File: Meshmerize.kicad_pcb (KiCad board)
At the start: 2 copper layers, 113.9 x 108.8 mm, 54 parts, among them J1 Conn_01x19_Male, J2 Conn_01x19_Male, J3 Conn_01x04_Female, M1 Motor_DC, M2 Motor_DC, U1 LM324, U2 ESP32-DEVKITC-32D, U3 TCRT5000, U4 TCRT5000, U5 MT3608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

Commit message: Added Logos
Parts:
- added G***: LOGO, logos:PCB_Power_Small, F.Cu at (183.6, 54.5)
- added G***: LOGO, logos:PCB-Power, B.Cu at (182.2, 65.0)
- added G***: LOGO, logos:KiCad, B.Cu at (122.6, 91.4)
- added G***: LOGO, logos:Open_Hardware, B.Cu at (184.1, 122.6)
- added G***: LOGO, SRA_Logo:sralogo, B.Cu at (161.7, 90.9)

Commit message: Added silkscreen, asset images, updated renders and gerbers
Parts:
- added G***: LOGO, SRA_Logo:sralogo, F.Cu at (164.4, 110.0)
- added REF**: OSHW-Logo2_9.8x8mm_SilkScreen, Symbol:OSHW-Logo2_9.8x8mm_SilkScreen, F.Cu at (137.8, 53.3)
- moved G*** 67.8 mm to (183.7, 54.9)
- moved G*** 52.0 mm to (181.1, 117.0)
- moved G*** 6.59 mm to (168.1, 92.4)
- moved G*** 0.48 mm to (183.5, 54.0)
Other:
- board text added: "Powered by"
- board text added: "SRA - VJTI"
- board text added: "Society of Robotics and Automation"
- board text removed: "Society of Robotics and Automation SRA - VJTI"

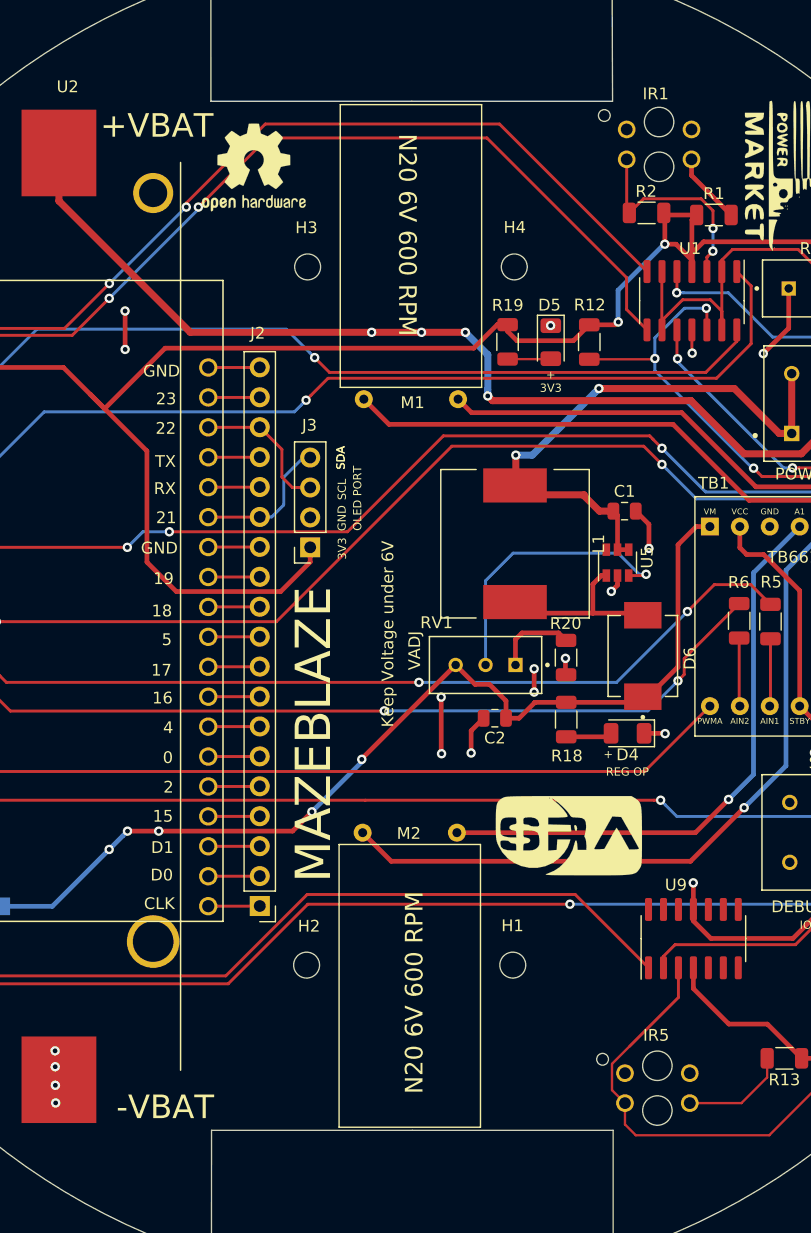
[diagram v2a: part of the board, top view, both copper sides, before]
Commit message: Fixed errors, optlized routing
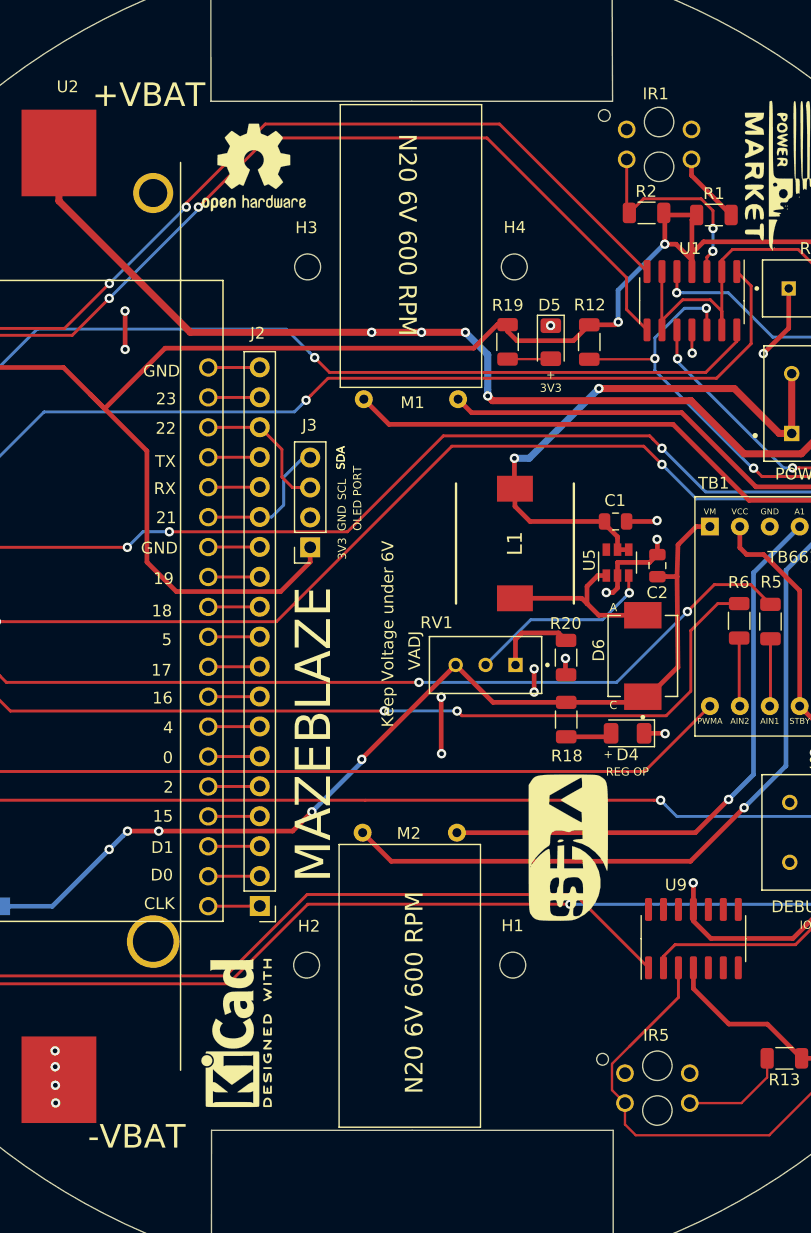
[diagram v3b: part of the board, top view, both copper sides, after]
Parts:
- added REF**: KiCad-Logo2_5mm_SilkScreen, Symbol:KiCad-Logo2_5mm_SilkScreen, F.Cu at (136.3, 126.8)
- L1: footprint Inductor_SMD:L_12x12mm_H6mm -> CDRH104RNP-220NC:INDPM102100X400N
- moved C2 18.9 mm to (172.0, 87.1), turned to 90 degrees
- moved C1 1.16 mm to (168.5, 83.4)
- moved G*** 1.10 mm to (164.4, 111.1), turned to 90 degrees
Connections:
- S1 pad 3: (no net) -> Net-(S1-Pad3)
- S1 pad 6: (no net) -> Net-(S1-Pad6)
- S2 pad 3: (no net) -> Net-(S2-Pad3)
- S2 pad 6: (no net) -> Net-(S2-Pad6)
- U5 pad 6: (no net) -> Net-(U5-Pad6)
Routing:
- net Net-(RV1-Pad2): track 24.0 -> 16.2 mm
- net A2: track 82.0 -> 84.5 mm
- net GND: track 76.6 -> 78.5 mm
- net SWO: track 49.9 -> 48.7 mm
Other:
- board text added: "A"
- board text added: "C"
